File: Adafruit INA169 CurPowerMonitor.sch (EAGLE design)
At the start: 12 parts, among them U1 INA169

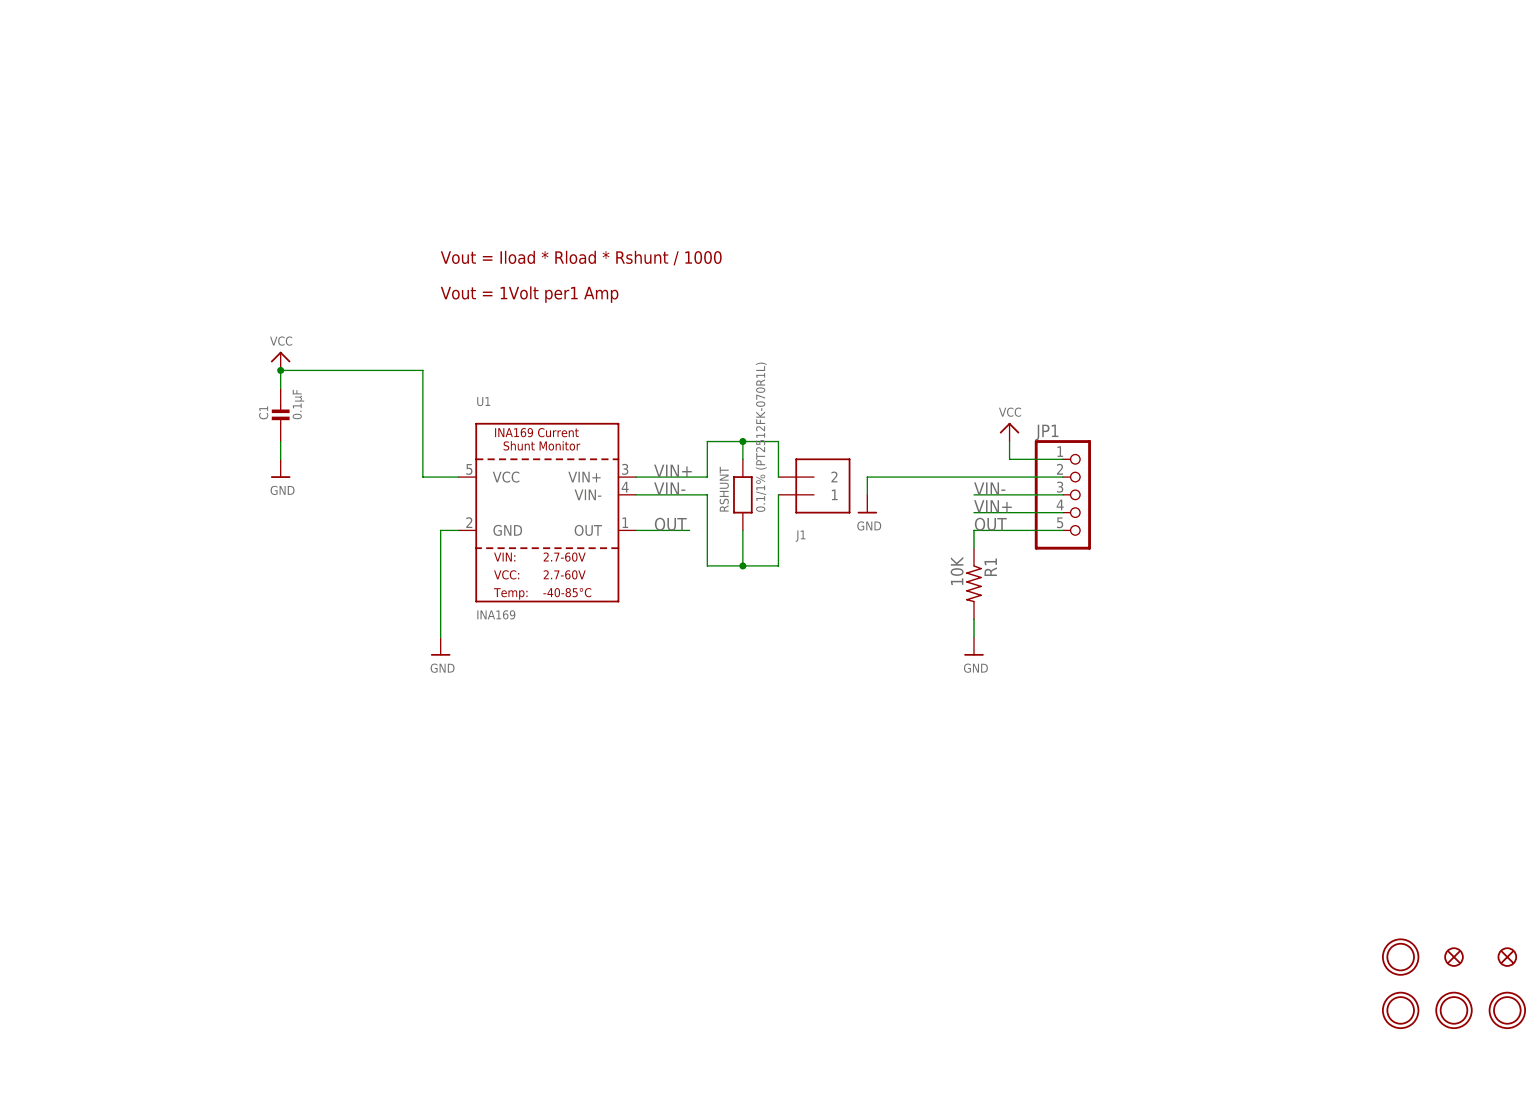
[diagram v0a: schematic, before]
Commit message: add load switch and rework for 24p DIL 600mil outline
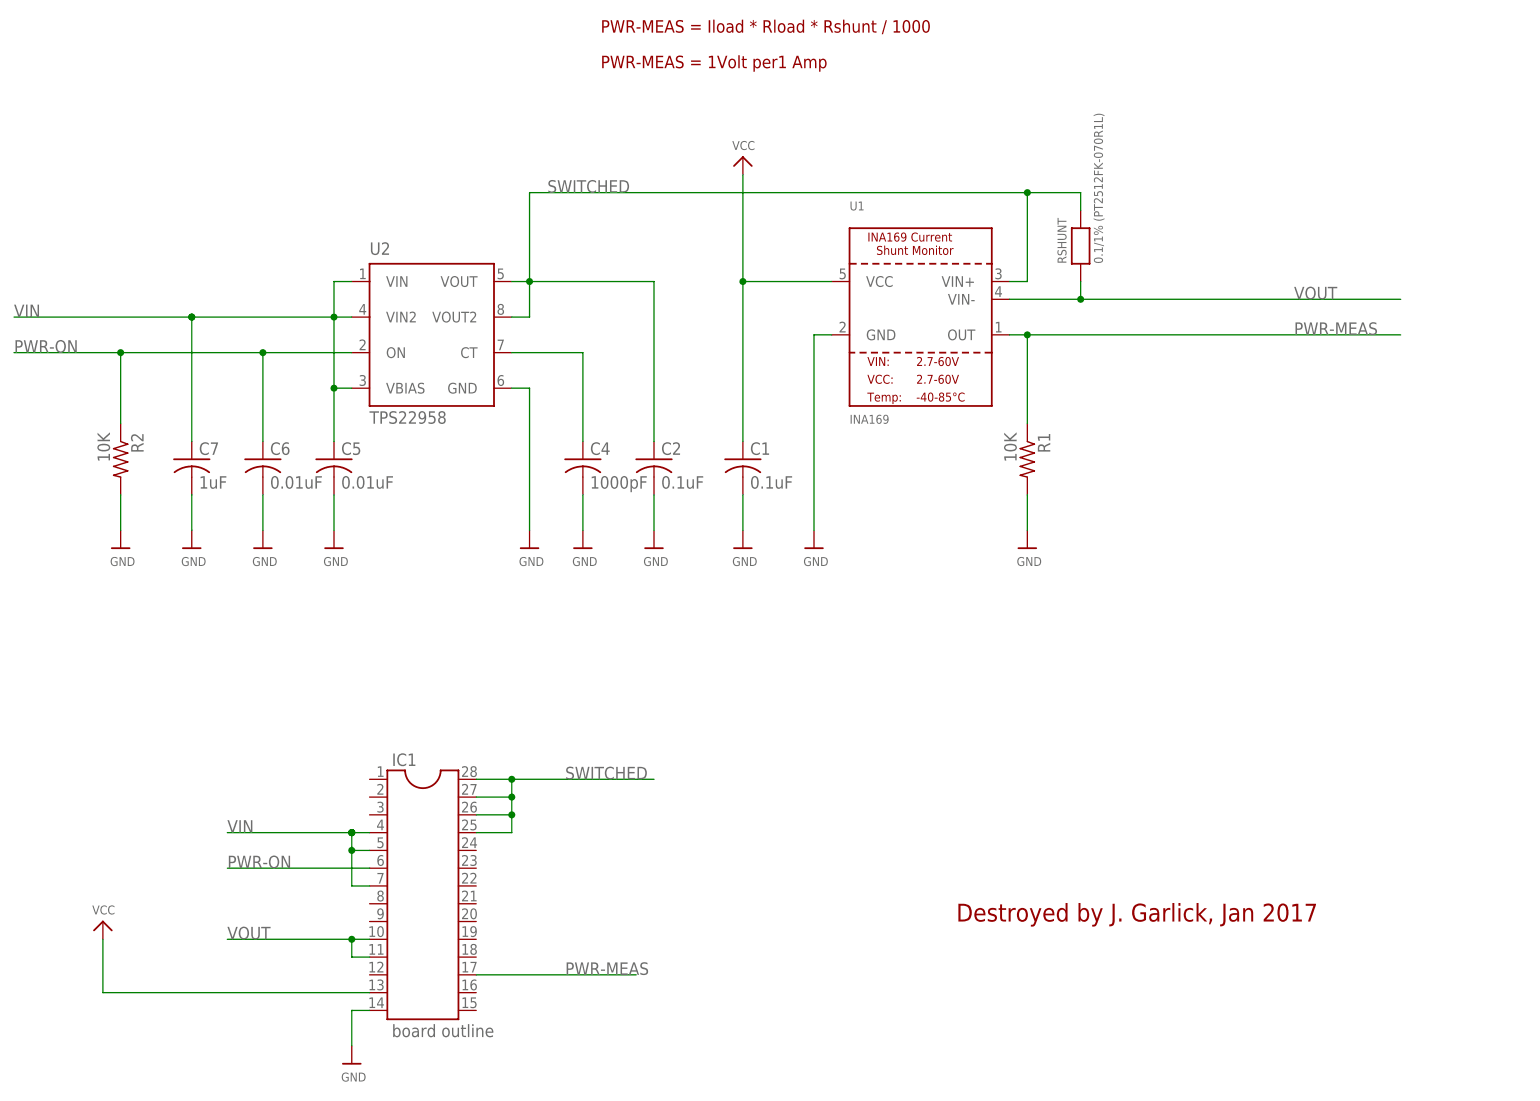
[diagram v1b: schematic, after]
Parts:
- removed FID1, FID2: FIDUCIAL"", microbuilder:FIDUCIAL""
- removed J1: (no value), microbuilder:TERMBLOCK_1X2
- removed JP1: (no value), microbuilder:HEADER-1X570MIL
- removed U$10, U$7, U$8, U$9: MOUNTINGHOLE2.5, microbuilder:MOUNTINGHOLE2.5
- added C2: 0.1uF, resistor:C-USC1206K
- added C4: 1000pF, resistor:C-USC1206K
- added C5, C6: 0.01uF, resistor:C-USC1206K
- added C7: 1uF, resistor:C-USC1206K
- added IC1: board outline, ic-package:DIL28
- added R2: 10K, resistor:R-US_M1206
- added U2: TPS22958, worlickwerx:TPS22958
- C1: value 0.1µF -> 0.1uF; device microbuilder:CAP_CERAMIC0805 -> resistor:C-USC1206K
- R1: device microbuilder:RESISTOR_DUAL -> resistor:R-US_M1206
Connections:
- removed net OUT: JP1.5, R1.1, U1.OUT
- removed net VIN+: J1.2, JP1.4, RSHUNT.2, U1.VIN+
- removed net VIN-: J1.1, JP1.3, RSHUNT.1, U1.VIN-
- new net CT: C4.1, U2.CT
- new net PWR-MEAS: IC1.17, R1.1, U1.OUT
- new net PWR-ON: C6.1, IC1.6, R2.1, U2.ON
- new net SWITCHED: C2.1, IC1.25, IC1.26, IC1.27, IC1.28, RSHUNT.2, U1.VIN+, U2.VOUT, U2.VOUT2
- new net VIN: C5.1, C7.1, IC1.4, IC1.5, IC1.7, U2.VBIAS, U2.VIN, U2.VIN2
- new net VOUT: IC1.10, IC1.11, RSHUNT.1, U1.VIN-
- net GND: now also C2.2, C4.2, C5.2, C6.2, C7.2, IC1.14, R2.2, U2.GND; no longer JP1.2
- net VCC: now also IC1.13; no longer JP1.1
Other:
- note added: "Destroyed by J. Garlick, Jan 2017"
- note added: "PWR-MEAS = 1Volt per1 Amp"
- note added: "PWR-MEAS = Iload * Rload * Rshunt / 1000"
- note removed: "Vout = 1Volt per1 Amp"
- note removed: "Vout = Iload * Rload * Rshunt / 1000"
- moved on the sheet: C1, R1, RSHUNT, U1
